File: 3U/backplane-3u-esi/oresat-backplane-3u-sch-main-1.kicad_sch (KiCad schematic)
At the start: 28 parts

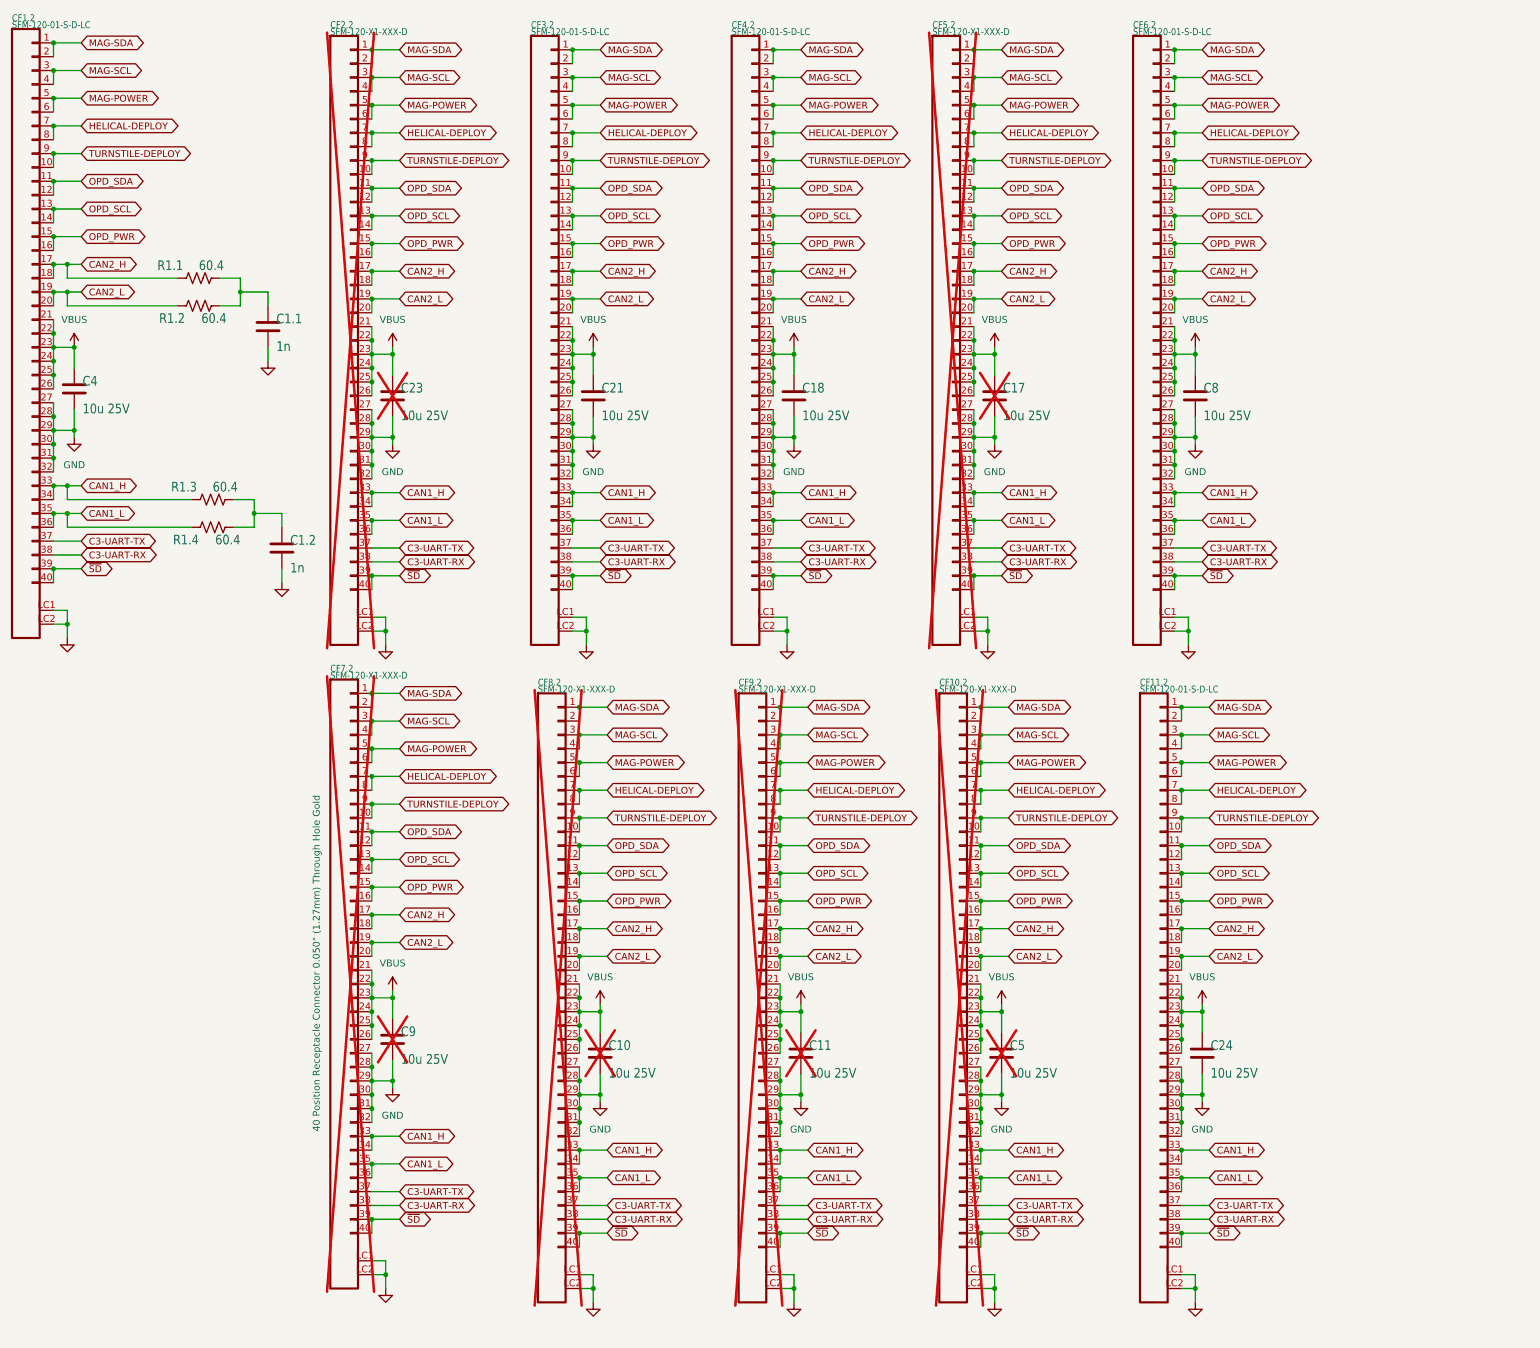
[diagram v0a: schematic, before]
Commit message: Changed schematic & pcb to add spare traces, no helical or turnstile
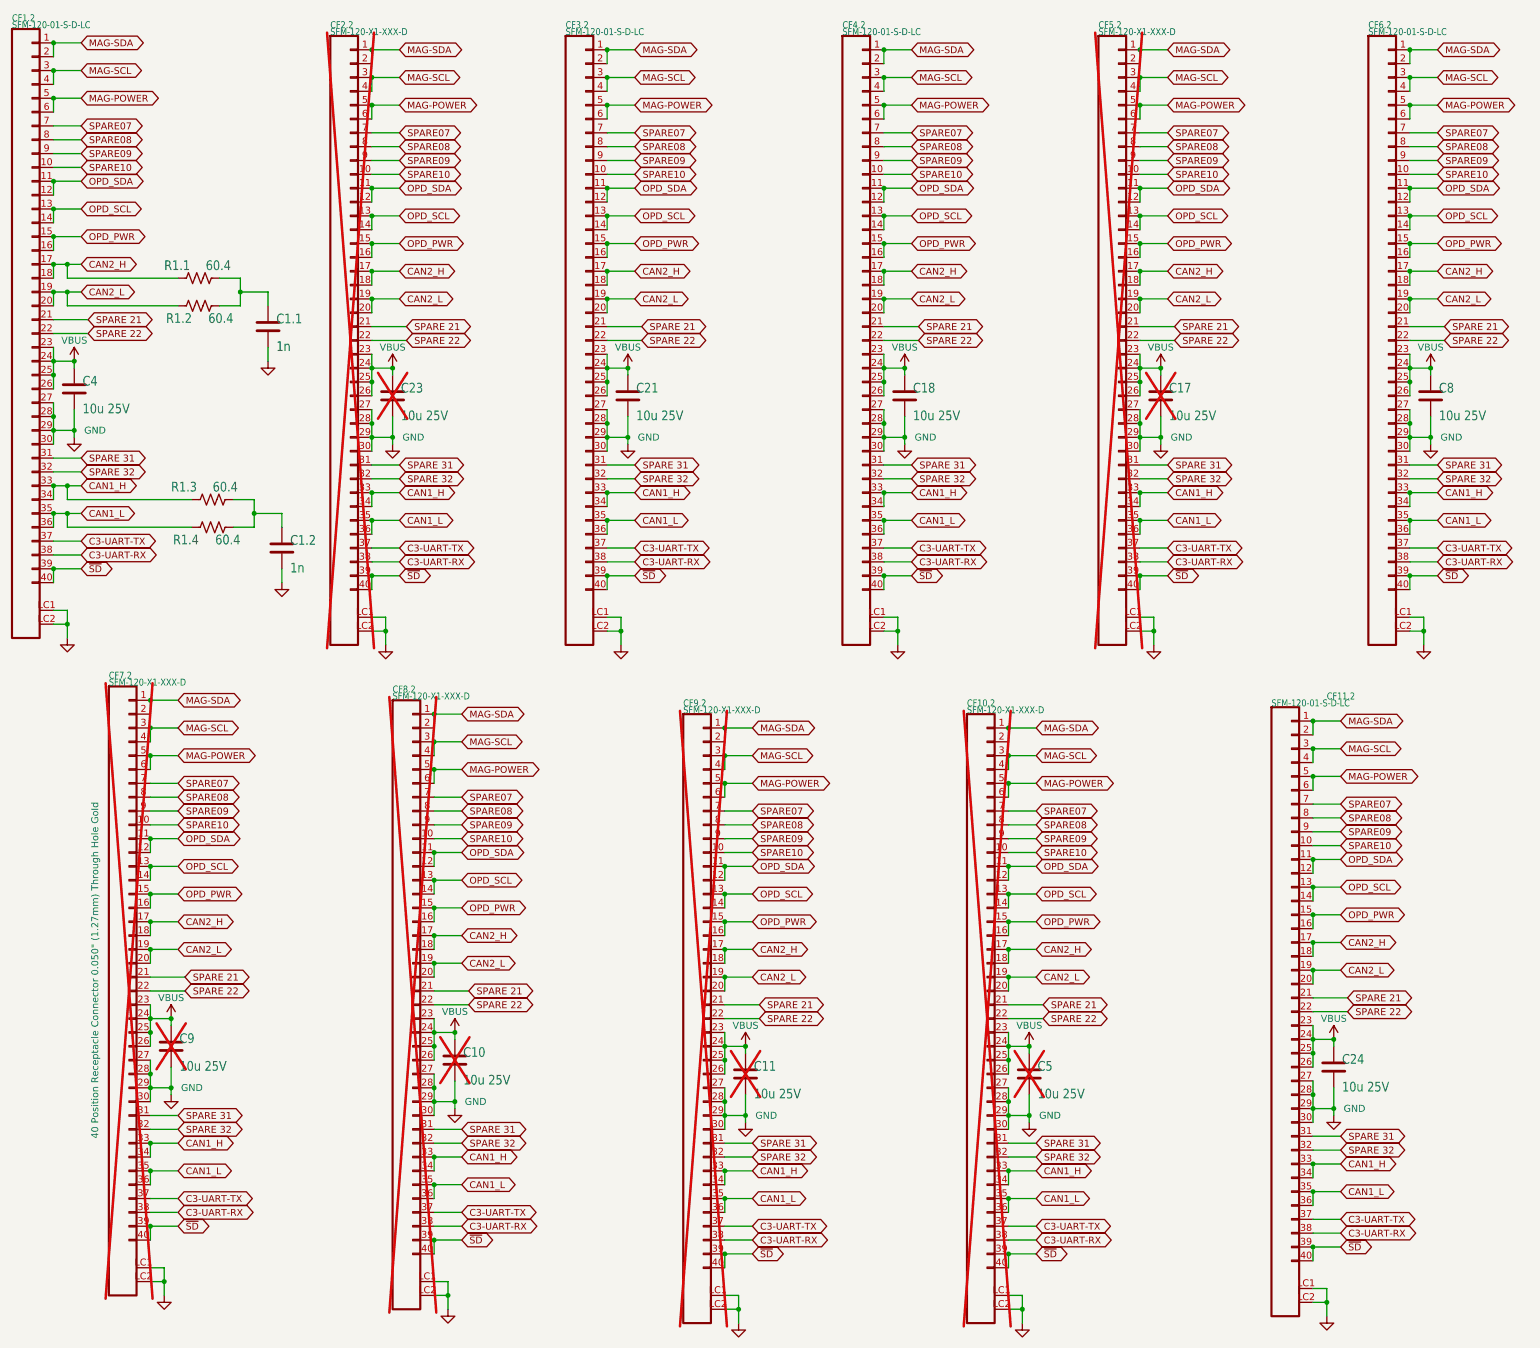
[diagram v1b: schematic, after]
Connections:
- net GND: no longer CF1.2.31, CF1.2.32, CF10.2.31, CF10.2.32, CF11.2.31, CF11.2.32, CF2.2.31, CF2.2.32, CF3.2.31, CF3.2.32, CF4.2.31, CF4.2.32, CF5.2.31, CF5.2.32, CF6.2.31, CF6.2.32, CF7.2.31, CF7.2.32, CF8.2.31, CF8.2.32, CF9.2.31, CF9.2.32
- net VBUS: no longer CF1.2.21, CF1.2.22, CF10.2.21, CF10.2.22, CF11.2.21, CF11.2.22, CF2.2.21, CF2.2.22, CF3.2.21, CF3.2.22, CF4.2.21, CF4.2.22, CF5.2.21, CF5.2.22, CF6.2.21, CF6.2.22, CF7.2.21, CF7.2.22, CF8.2.21, CF8.2.22, CF9.2.21, CF9.2.22
- net HELICAL-DEPLOY renamed SPARE07
- net SPARE07: no longer CF1.2.8, CF10.2.8, CF11.2.8, CF2.2.8, CF3.2.8, CF4.2.8, CF5.2.8, CF6.2.8, CF7.2.8, CF8.2.8, CF9.2.8
- net TURNSTILE-DEPLOY renamed SPARE09
- net SPARE09: no longer CF1.2.10, CF10.2.10, CF11.2.10, CF2.2.10, CF3.2.10, CF4.2.10, CF5.2.10, CF6.2.10, CF7.2.10, CF8.2.10, CF9.2.10
- new net SPARE 21: CF1.2.21, CF10.2.21, CF11.2.21, CF2.2.21, CF3.2.21, CF4.2.21, CF5.2.21, CF6.2.21, CF7.2.21, CF8.2.21, CF9.2.21
- new net SPARE 22: CF1.2.22, CF10.2.22, CF11.2.22, CF2.2.22, CF3.2.22, CF4.2.22, CF5.2.22, CF6.2.22, CF7.2.22, CF8.2.22, CF9.2.22
- new net SPARE 31: CF1.2.31, CF10.2.31, CF11.2.31, CF2.2.31, CF3.2.31, CF4.2.31, CF5.2.31, CF6.2.31, CF7.2.31, CF8.2.31, CF9.2.31
- new net SPARE 32: CF1.2.32, CF10.2.32, CF11.2.32, CF2.2.32, CF3.2.32, CF4.2.32, CF5.2.32, CF6.2.32, CF7.2.32, CF8.2.32, CF9.2.32
- new net SPARE08: CF1.2.8, CF10.2.8, CF11.2.8, CF2.2.8, CF3.2.8, CF4.2.8, CF5.2.8, CF6.2.8, CF7.2.8, CF8.2.8, CF9.2.8
- new net SPARE10: CF1.2.10, CF10.2.10, CF11.2.10, CF2.2.10, CF3.2.10, CF4.2.10, CF5.2.10, CF6.2.10, CF7.2.10, CF8.2.10, CF9.2.10
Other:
- moved on the sheet: CF10.2, CF11.2, CF3.2, CF4.2, CF5.2, CF6.2, CF7.2, CF8.2, CF9.2

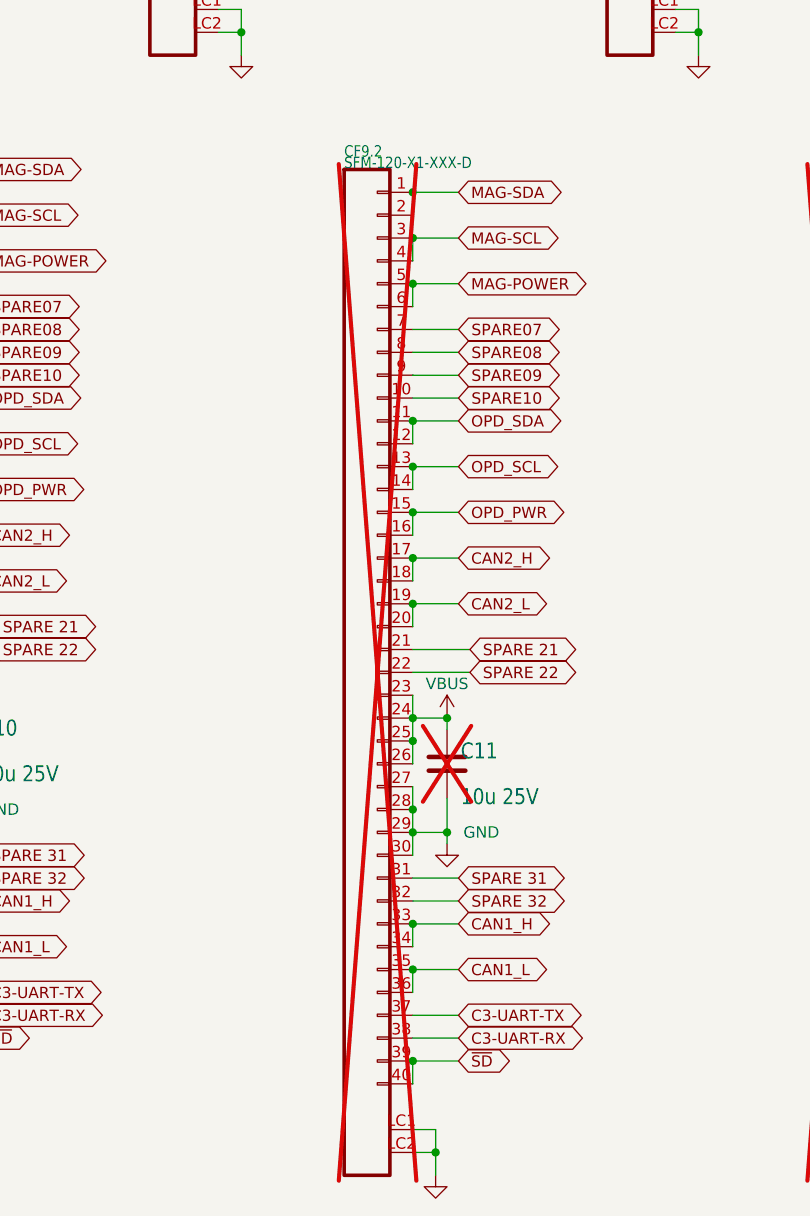
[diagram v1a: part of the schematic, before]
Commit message: Changed DNP for SDR control board
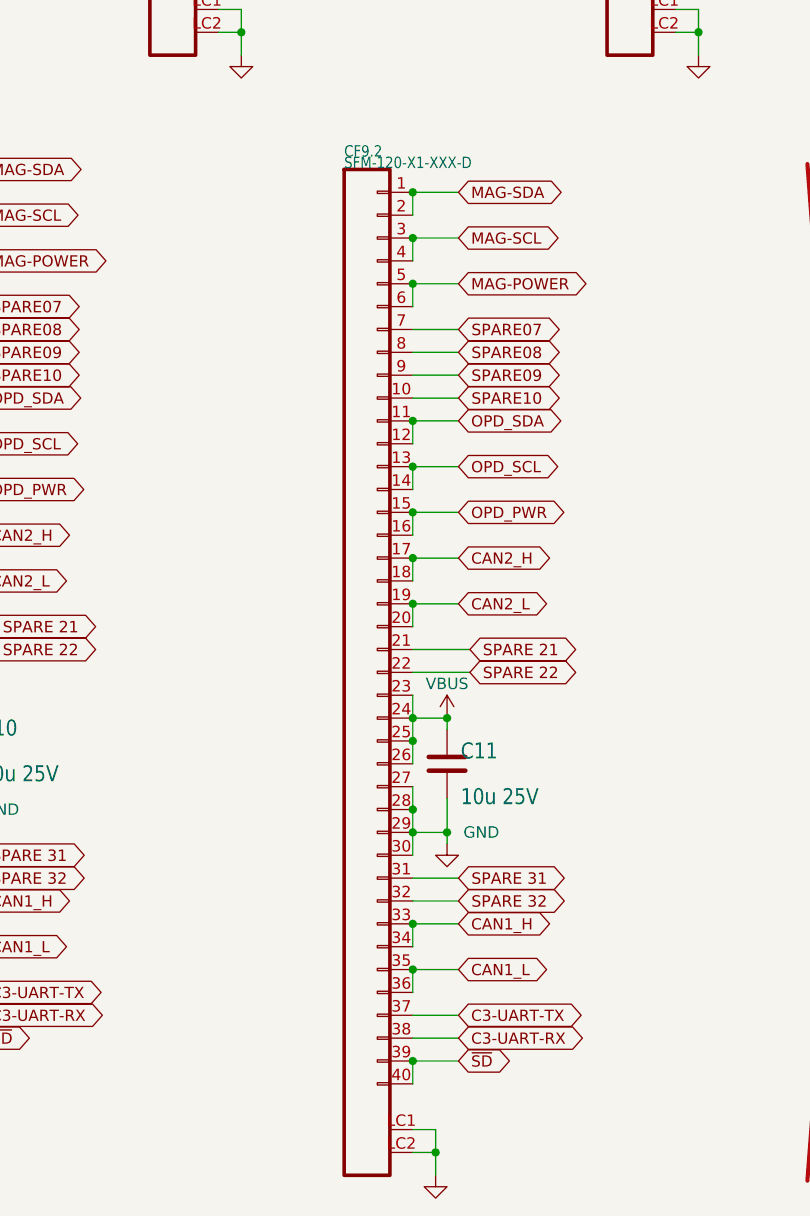
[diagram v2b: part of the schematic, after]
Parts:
- C11, CF9.2: now fitted
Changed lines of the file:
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@@
 		(in_bom yes)
 		(on_board yes)
-		(dnp yes)
+		(dnp no)
 		(property "Reference" "CF9.2"
 			(at 224.79 147.32 0)
@@
 		(in_bom yes)
 		(on_board yes)
-		(dnp yes)
+		(dnp no)
 		(property "Reference" "C11"
 			(at 237.744 214.249 0)
